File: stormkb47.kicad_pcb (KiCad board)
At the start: 2 copper layers, 95 parts, among them J1 Conn_02x20_Odd_Even

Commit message: align keys and change labels to read the keycaps
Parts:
- MX1: value MX-NoLED -> Esc ~ `
- MX10: value MX-NoLED -> O ( 9
- MX11: value MX-NoLED -> P ) 0
- MX12: value MX-NoLED -> { [ _ -
- MX13: value MX-NoLED -> } ] + =
- MX14: value MX-NoLED -> Tab
- MX15: value MX-NoLED -> A F1
- MX16: value MX-NoLED -> S F2
- MX17: value MX-NoLED -> D F3
- MX18: value MX-NoLED -> F F4
- MX19: value MX-NoLED -> G F5
- MX2: value MX-NoLED -> Q ! 1
- MX20: value MX-NoLED -> H F6
- MX21: value MX-NoLED -> J F7
- MX22: value MX-NoLED -> K F8
- MX23: value MX-NoLED -> L F9
- MX24: value MX-NoLED -> : ; " '
- MX25: value MX-NoLED -> Enter
- MX26: value MX-NoLED -> Shift
- MX27: value MX-NoLED -> Z Ins
- MX28: value MX-NoLED -> X Del
- MX29: value MX-NoLED -> C Break
- MX3: value MX-NoLED -> W @ 2
- MX30: value MX-NoLED -> V Pause
- MX31: value MX-NoLED -> B PrtSc
- MX32: value MX-NoLED -> N SysRq
- MX33: value MX-NoLED -> M F10
- MX34: value MX-NoLED -> < , F11
- MX35: value MX-NoLED -> > , F12
- MX36: value MX-NoLED -> UpArr PgUp
- MX37: value MX-NoLED -> ? /
- MX38: value MX-NoLED -> Ctrl
- MX39: value MX-NoLED -> Fn
- MX4: value MX-NoLED -> E # 3
- MX40: value MX-NoLED -> Meta
- MX42: value MX-NoLED -> Space
- MX43: value MX-NoLED -> AltGr
- MX44: value MX-NoLED -> | \
- MX45: value MX-NoLED -> LArr Home
- MX46: value MX-NoLED -> DnArr PgDn
- MX47: value MX-NoLED -> RArr End
- MX5: value MX-NoLED -> R $ 4
- MX6: value MX-NoLED -> T % 5
- MX7: value MX-NoLED -> Y ^ 6
- MX8: value MX-NoLED -> U & 7
- MX9: value MX-NoLED -> I * 8
- moved D1 382.4 mm to (66.0, 147.2)
- moved D10 382.4 mm to (66.0, 177.3)
- moved D11 382.4 mm to (71.8, 147.2)
- moved D12 382.4 mm to (71.8, 150.5)
- moved D13 382.4 mm to (71.8, 153.8)
- moved D14 382.4 mm to (71.8, 157.2)
- moved D15 382.4 mm to (71.8, 160.6)
- moved D16 382.4 mm to (71.8, 163.9)
- moved D17 382.4 mm to (71.8, 167.2)
- moved D18 382.4 mm to (71.8, 170.6)
- moved D19 382.4 mm to (71.8, 173.9)
- moved D2 382.4 mm to (66.0, 150.5)
- moved D20 382.4 mm to (71.8, 177.3)
- moved D21 382.4 mm to (77.6, 147.2)
- moved D22 382.4 mm to (77.6, 150.5)
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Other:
- board outline added: 257.7 x 109.2 mm

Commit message: diodes placed
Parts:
- moved D13 223.8 mm to (272.4, 54.4), turned to 90 degrees
- moved D25 208.9 mm to (267.6, 73.6), turned to 90 degrees
- moved D12 205.3 mm to (253.3, 54.4), turned to 90 degrees
- moved D37 202.9 mm to (272.1, 92.6), turned to 90 degrees
- moved D10 193.3 mm to (215.2, 54.4), turned to 90 degrees
- moved D47 191.1 mm to (272.1, 111.7), turned to 90 degrees
- moved D11 187.0 mm to (234.3, 54.4), turned to 90 degrees
- moved D24 186.0 mm to (243.8, 73.7), turned to 90 degrees
- moved D36 183.9 mm to (253.0, 92.6), turned to 90 degrees
- moved D9 176.7 mm to (195.9, 54.1), turned to 90 degrees
- moved D46 171.9 mm to (253.0, 111.7), turned to 90 degrees
- moved D23 167.3 mm to (224.7, 74.2), turned to 90 degrees
- moved D35 165.4 mm to (234.3, 92.6), turned to 90 degrees
- moved D8 161.0 mm to (177.1, 54.1), turned to 90 degrees
- moved D45 153.2 mm to (234.3, 111.4), turned to 90 degrees
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
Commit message: routed all traces
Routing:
- net ROW4: track 0.00 -> 430.8 mm
- net ROW2: track 0.00 -> 395.7 mm
- net ROW3: track 0.00 -> 375.5 mm
- net ROW1: track 0.00 -> 251.7 mm
- net COL13: track 0.00 -> 169.4 mm
- net COL1: track 0.00 -> 161.0 mm
- net COL12: track 0.00 -> 148.5 mm
- net COL11: track 0.00 -> 140.6 mm
- net COL3: track 0.00 -> 130.9 mm
- net COL10: track 0.00 -> 123.2 mm
- net COL9: track 0.00 -> 108.0 mm
- net COL7: track 0.00 -> 79.3 mm
- net COL5: track 0.00 -> 77.7 mm
- net COL4: track 0.00 -> 65.0 mm
- net COL2: track 0.00 -> 63.0 mm
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
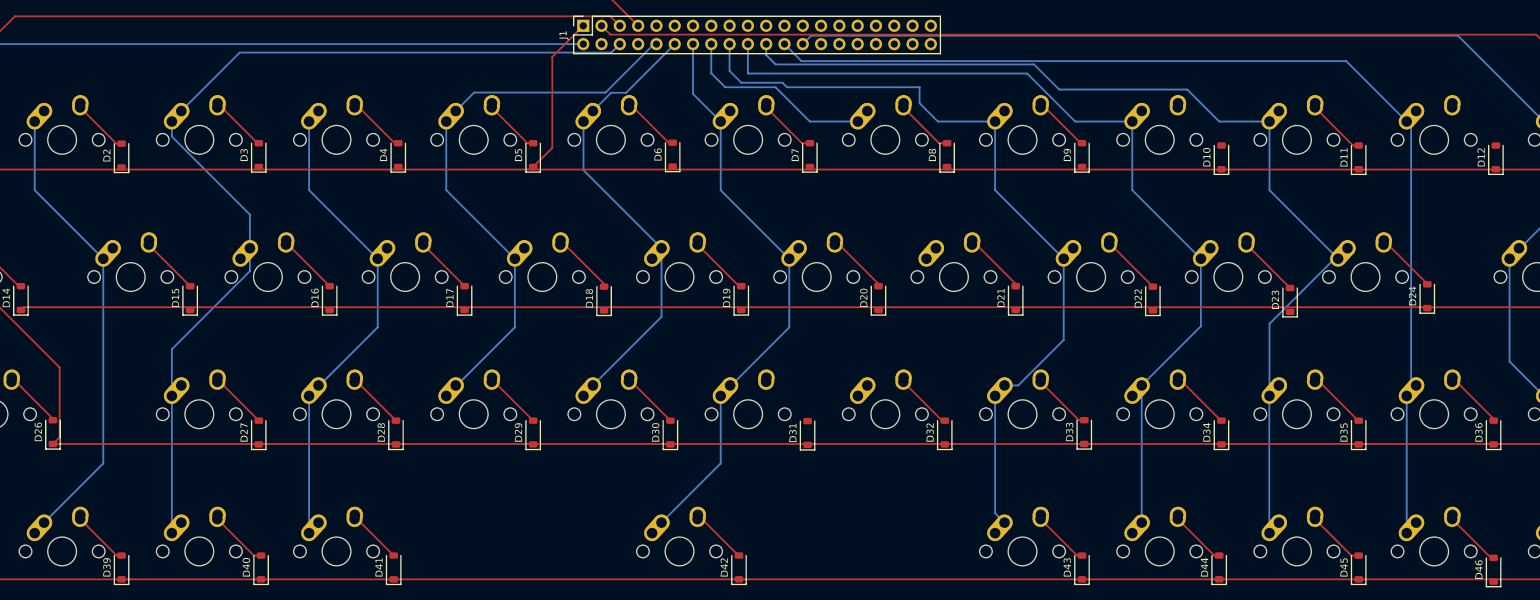
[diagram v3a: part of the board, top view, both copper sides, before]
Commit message: fixed missing connections
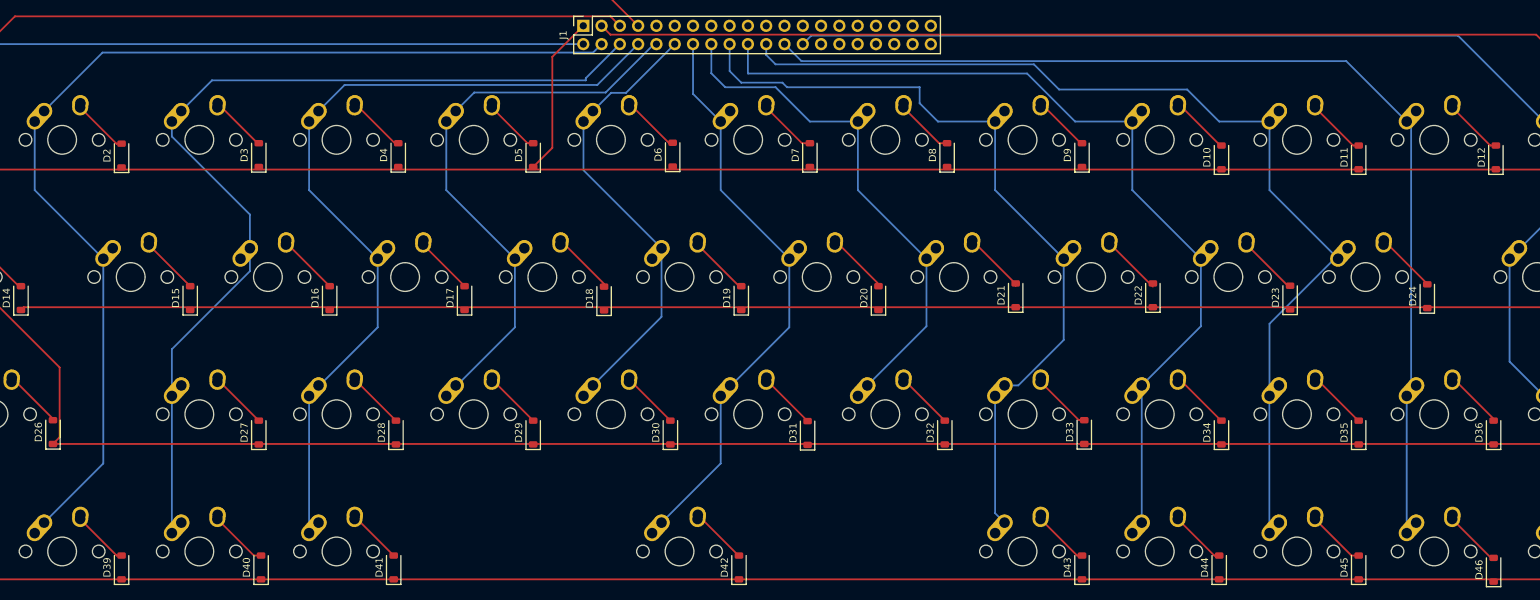
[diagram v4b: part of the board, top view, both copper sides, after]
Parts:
- moved D22 0.44 mm to (205.7, 73.6)
- moved D21 0.38 mm to (186.6, 73.6)
- moved D23 0.32 mm to (224.7, 73.9)
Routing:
- net COL2: track 63.0 -> 144.3 mm
- net COL4: track 65.0 -> 113.3 mm
- net COL8: track 27.2 -> 71.2 mm
- net Net-(D10-A): track 0.00 -> 8.46 mm
- net Net-(D31-A): track 0.00 -> 8.33 mm
- net Net-(D12-A): track 0.00 -> 8.26 mm
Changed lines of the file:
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@@
   )
   (footprint "Diode_SMD:D_SOD-123" (layer "F.Cu")
-    (at 186.6475 73.97 90)
+    (at 186.6475 73.59 90)
     (descr "SOD-123")
     (tags "SOD-123")
@@
   )
   (footprint "Diode_SMD:D_SOD-123" (layer "F.Cu")
-    (at 224.7475 74.225 90)
+    (at 224.7475 73.9075 90)
     (descr "SOD-123")
     (tags "SOD-123")
@@
   )
   (footprint "Diode_SMD:D_SOD-123" (layer "F.Cu")
-    (at 205.6975 74.0325 90)
+    (at 205.6975 73.59 90)
     (descr "SOD-123")
     (tags "SOD-123")
@@
   (segment (start 195.69 52.47) (end 195.855 52.47) (width 0.25) (layer "F.Cu") (net 10))
   (segment (start 190.14 46.92) (end 195.69 52.47) (width 0.25) (layer "F.Cu") (net 10))
+  (segment (start 215.0575 52.7875) (end 215.2225 52.7875) (width 0.25) (layer "F.Cu") (net 11))
+  (segment (start 209.19 46.92) (end 215.0575 52.7875) (width 0.25) (layer "F.Cu") (net 11))
   (segment (start 233.4875 52.7875) (end 234.2725 52.7875) (width 0.25) (layer "F.Cu") (net 12))
   (segment (start 228.2 47.5) (end 233.4875 52.7875) (width 0.25) (layer "F.Cu") (net 12))
+  (segment (start 252.5375 52.7875) (end 253.3225 52.7875) (width 0.25) (layer "F.Cu") (net 13))
+  (segment (start 247.25 47.5) (end 252.5375 52.7875) (width 0.25) (layer "F.Cu") (net 13))
   (segment (start 266.3 47.5) (end 271.5875 52.7875) (width 0.25) (layer "F.Cu") (net 14))
   (segment (start 271.5875 52.7875) (end 272.3725 52.7875) (width 0.25) (layer "F.Cu") (net 14))
@@
   (segment (start 132.95 85.6) (end 133.315 85.6) (width 0.25) (layer "F.Cu") (net 33))
   (segment (start 133.315 85.6) (end 138.705 90.99) (width 0.25) (layer "F.Cu") (net 33))
-  (segment (start 171.05 85.6) (end 176.44 90.99) (width 0.25) (layer "F.Cu") (net 35))
+  (segment (start 152 85.6) (end 152.3025 85.6) (width 0.25) (layer "F.Cu") (net 34))
+  (segment (start 152.3025 85.6) (end 157.755 91.0525) (width 0.25) (layer "F.Cu") (net 34))
+  (segment (start 157.755 90.735) (end 157.755 91.0525) (width 0.25) (layer "F.Cu") (net 34))
+  (segment (start 171.05 85.6) (end 171.415 85.6) (width 0.25) (layer "F.Cu") (net 35))
+  (segment (start 171.415 85.6) (end 176.805 90.99) (width 0.25) (layer "F.Cu") (net 35))
   (segment (start 176.44 90.99) (end 176.805 90.99) (width 0.25) (layer "F.Cu") (net 35))
   (segment (start 190.1 85.6) (end 195.4275 90.9275) (width 0.25) (layer "F.Cu") (net 36))
@@
   (segment (start 142.515 104.07) (end 148.1675 109.7225) (width 0.25) (layer "F.Cu") (net 46))
   (segment (start 148.1675 109.7225) (end 148.23 109.7225) (width 0.25) (layer "F.Cu") (net 46))
-  (segment (start 190.1 104.65) (end 195.1725 109.7225) (width 0.25) (layer "F.Cu") (net 47))
-  (segment (start 195.1725 109.7225) (end 195.855 109.7225) (width 0.25) (layer "F.Cu") (net 47))
+  (segment (start 195.855 109.7225) (end 195.1725 109.7225) (width 0.25) (layer "F.Cu") (net 47))
+  (segment (start 195.1725 109.7225) (end 190.1 104.65) (width 0.25) (layer "F.Cu") (net 47))
   (segment (start 214.2225 109.7225) (end 214.905 109.7225) (width 0.25) (layer "F.Cu") (net 48))
   (segment (start 209.15 104.65) (end 214.2225 109.7225) (width 0.25) (layer "F.Cu") (net 48))
@@
   (segment (start 41.99 38.71) (end 126.61 38.71) (width 0.25) (layer "B.Cu") (net 52))
   (segment (start 50.44 49.46) (end 50.44 58.985) (width 0.25) (layer "B.Cu") (net 53))
+  (segment (start 127.975 39.885) (end 129.15 38.71) (width 0.25) (layer "B.Cu") (net 53))
   (segment (start 59.965 96.935) (end 51.75 105.15) (width 0.25) (layer "B.Cu") (net 53))
   (segment (start 50.44 58.985) (end 59.965 68.51) (width 0.25) (layer "B.Cu") (net 53))
+  (segment (start 59.865 39.885) (end 127.975 39.885) (width 0.25) (layer "B.Cu") (net 53))
   (segment (start 59.965 68.51) (end 59.965 96.935) (width 0.25) (layer "B.Cu") (net 53))
+  (segment (start 51.75 48) (end 59.865 39.885) (width 0.25) (layer "B.Cu") (net 53))
   (segment (start 80.325 62.375131) (end 80.325 67.05) (width 0.25) (layer "B.Cu") (net 54))
   (segment (start 69.49 51.540131) (end 80.325 62.375131) (width 0.25) (layer "B.Cu") (net 54))
   (segment (start 80.325 70.237767) (end 69.49 81.072767) (width 0.25) (layer "B.Cu") (net 54))
+  (segment (start 131.69 38.71) (end 126.9575 43.4425) (width 0.25) (layer "B.Cu") (net 54))
   (segment (start 69.49 81.072767) (end 69.49 87.56) (width 0.25) (layer "B.Cu") (net 54))
   (segment (start 69.49 87.56) (end 69.49 106.61) (width 0.25) (layer "B.Cu") (net 54))
   (segment (start 80.325 67.05) (end 80.325 70.237767) (width 0.25) (layer "B.Cu") (net 54))
-  (segment (start 70.8 48) (end 78.915 39.885) (width 0.25) (layer "B.Cu") (net 54))
   (segment (start 69.49 49.46) (end 69.49 51.540131) (width 0.25) (layer "B.Cu") (net 54))
-  (segment (start 78.915 39.885) (end 130.515 39.885) (width 0.25) (layer "B.Cu") (net 54))
-  (segment (start 130.515 39.885) (end 131.69 38.71) (width 0.25) (layer "B.Cu") (net 54))
+  (segment (start 126.9575 43.745) (end 75.055 43.745) (width 0.25) (layer "B.Cu") (net 54))
+  (segment (start 75.055 43.745) (end 70.8 48) (width 0.25) (layer "B.Cu") (net 54))
+  (segment (start 126.9575 43.4425) (end 126.9575 43.745) (width 0.25) (layer "B.Cu") (net 54))
   (segment (start 88.54 87.56) (end 88.54 106.61) (width 0.25) (layer "B.Cu") (net 55))
   (segment (start 98.065 68.51) (end 98.065 78.035) (width 0.25) (layer "B.Cu") (net 55))
+  (segment (start 93.47 44.38) (end 89.85 48) (width 0.25) (layer "B.Cu") (net 55))
   (segment (start 98.065 78.035) (end 88.54 87.56) (width 0.25) (layer "B.Cu") (net 55))
   (segment (start 88.54 58.985) (end 98.065 68.51) (width 0.25) (layer "B.Cu") (net 55))
+  (segment (start 134.23 38.71) (end 128.56 44.38) (width 0.25) (layer "B.Cu") (net 55))
+  (segment (start 128.56 44.38) (end 93.47 44.38) (width 0.25) (layer "B.Cu") (net 55))
   (segment (start 88.54 49.46) (end 88.54 58.985) (width 0.25) (layer "B.Cu") (net 55))
   (segment (start 136.4375 38.71) (end 136.77 38.71) (width 0.25) (layer "B.Cu") (net 57))
@@
   (segment (start 155.215 78.035) (end 145.69 87.56) (width 0.25) (layer "B.Cu") (net 61))
   (segment (start 155.215 68.51) (end 155.215 78.035) (width 0.25) (layer "B.Cu") (net 61))
+  (segment (start 164.74 58.985) (end 174.265 68.51) (width 0.25) (layer "B.Cu") (net 63))
+  (segment (start 166.05 86.1) (end 174.265 77.885) (width 0.25) (layer "B.Cu") (net 63))
   (segment (start 164.74 49.46) (end 158.0725 49.46) (width 0.25) (layer "B.Cu") (net 63))
+  (segment (start 164.74 49.46) (end 164.74 58.985) (width 0.25) (layer "B.Cu") (net 63))
   (segment (start 146.325 44.6975) (end 144.39 42.7625) (width 0.25) (layer "B.Cu") (net 63))
   (segment (start 153.31 44.6975) (end 146.325 44.6975) (width 0.25) (layer "B.Cu") (net 63))
+  (segment (start 174.265 77.885) (end 174.265 68.51) (width 0.25) (layer "B.Cu") (net 63))
   (segment (start 144.39 42.7625) (end 144.39 38.71) (width 0.25) (layer "B.Cu") (net 63))
   (segment (start 158.0725 49.46) (end 153.31 44.6975) (width 0.25) (layer "B.Cu") (net 63))

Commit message: move spacebar and add 48th key
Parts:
- added D44: D_Small, Diode_SMD:D_SOD-123, F.Cu at (196.2, 111.4)
- added MX43: Menu, MX_Alps_Hybrid:MX-1U-NoLED, F.Cu at (168.6, 109.2)
- MX13: value } ] + = -> ] } + =
- MX14, MX25: footprint MX_Alps_Hybrid:MX-1U-NoLED -> MX_Alps_Hybrid:MX-1.5U-NoLED
- MX24: value : ; " ' -> ; : " '
- MX26: footprint MX_Alps_Hybrid:MX-1U-NoLED -> MX_Alps_Hybrid:MX-2U-NoLED
- MX35: value > , F12 -> > . F12
- MX41: value MX-NoLED -> Alt
- MX42: footprint MX_Alps_Hybrid:MX-1U-NoLED -> MX_Alps_Hybrid:MX-3U-NoLED
- MX46: renamed from MX45; value LArr Home -> ArrL Home
- MX47: renamed from MX46; value DnArr PgDn -> ArrDn PgDn
- MX48: renamed from MX47; value RArr End -> ArrR End
- moved D43 18.7 mm to (177.1, 111.1)
- moved MX42 9.53 mm to (130.4, 109.2)
- moved D42 9.52 mm to (138.7, 111.4)
- renumbered D44 to D45, D45 to D46, D46 to D47, D47 to D48, MX43 to MX44, MX44 to MX45
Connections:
- MX42 pad 1: COL7 -> COL6
- MX44 pad 2: Net-(D43-A) -> Net-(D44-A)
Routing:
- net COL7: track 79.3 -> 58.3 mm
- net COL8: track 71.2 -> 90.2 mm
- net COL6: track 60.3 -> 78.4 mm
- net Net-(D44-A): track 0.00 -> 7.86 mm

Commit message: logo and annotations on silkscreen layer
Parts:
- added REF**: MountingHole_3.2mm_M3, MountingHole:MountingHole_3.2mm_M3, F.Cu at (28.1, 126.2)
- added REF**: MountingHole_3.2mm_M3, MountingHole:MountingHole_3.2mm_M3, F.Cu at (28.2, 31.9)
- added REF**: MountingHole_3.2mm_M3, MountingHole:MountingHole_3.2mm_M3, F.Cu at (270.7, 126.1)
- added REF**: MountingHole_3.2mm_M3, MountingHole:MountingHole_3.2mm_M3, F.Cu at (270.8, 32.0)
- added REF**: MountingHole_3.2mm_M3, MountingHole:MountingHole_3.2mm_M3, F.Cu at (149.5, 126.2)
- added REF**: MountingHole_3.2mm_M3, MountingHole:MountingHole_3.2mm_M3, F.Cu at (149.5, 32.0)
- MX43: value Menu -> AltGr
- MX44: value AltGr -> Menu
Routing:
- net COL2: track 144.3 -> 145.1 mm
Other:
- outline, holes or cut-outs redrawn
- board text added: "STORMKB47 1.0"
